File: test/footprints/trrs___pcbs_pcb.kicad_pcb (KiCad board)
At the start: 2 copper layers, 3 parts

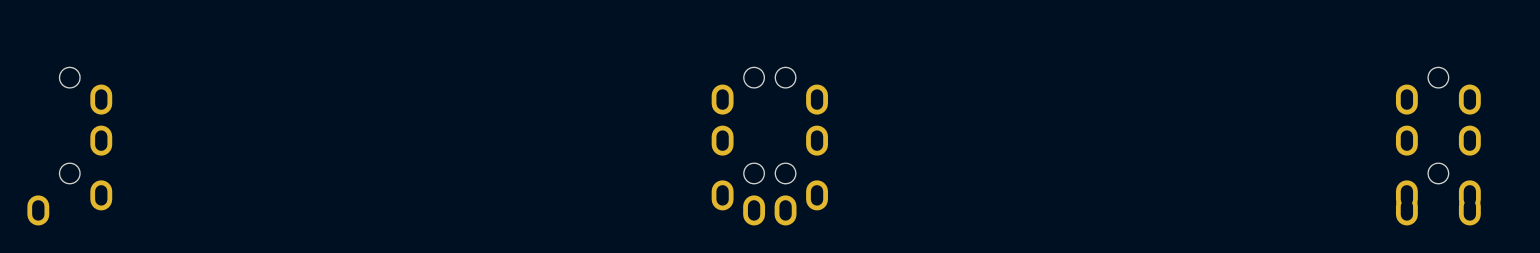
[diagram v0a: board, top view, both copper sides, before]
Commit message: TEST: Fix tests for new power netclass
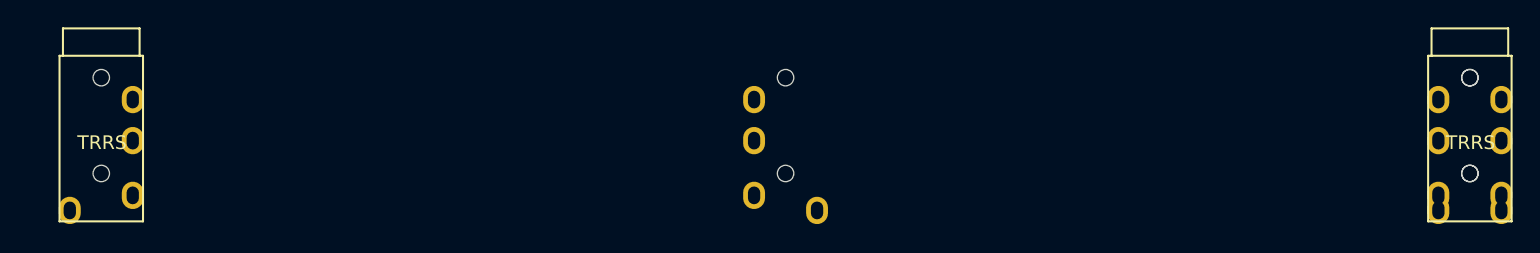
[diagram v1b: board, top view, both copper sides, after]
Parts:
- removed TRRS1, TRRS2, TRRS3: TRRS-PJ-320A-dual, TRRS-PJ-320A-dual
- added TRRS_B: AudioJack4, TRRS-PJ-320A-dual, B.Cu at (50.0, 0.00)
- added TRRS_B: AudioJack4, TRRS-PJ-320A-dual, B.Cu at (100.0, 0.00)
- added TRRS_F: AudioJack4, TRRS-PJ-320A-dual, F.Cu at (0.00, 0.00)
- added TRRS_F: AudioJack4, TRRS-PJ-320A-dual, F.Cu at (100.0, 0.00)
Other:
- net class Power added: clearance 0.2, trace_width 0.5, via_dia 0.8, via_drill 0.4
